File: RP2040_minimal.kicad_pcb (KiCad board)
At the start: 2 copper layers, 52 x 51 mm, 34 parts, among them J1 USB_B_Micro, J2 Conn_01x02, J3 Conn_02x18_Odd_Even, J4 Conn_02x18_Odd_Even, U1 NCP1117-3.3_SOT223, U2 W25Q128JVS, U3 RP2040, Y1 ABLS-12.000MHZ-B4-T

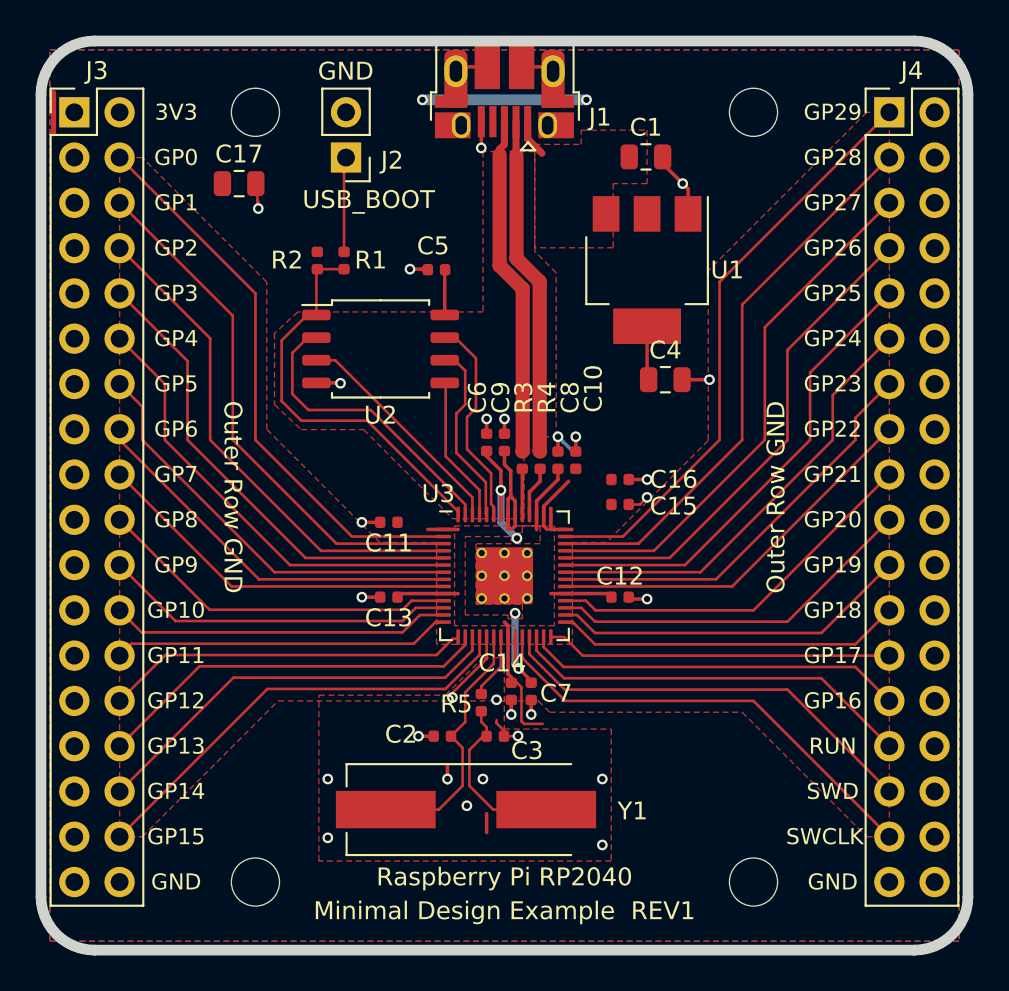
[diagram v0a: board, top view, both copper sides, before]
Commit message: get DRC passing
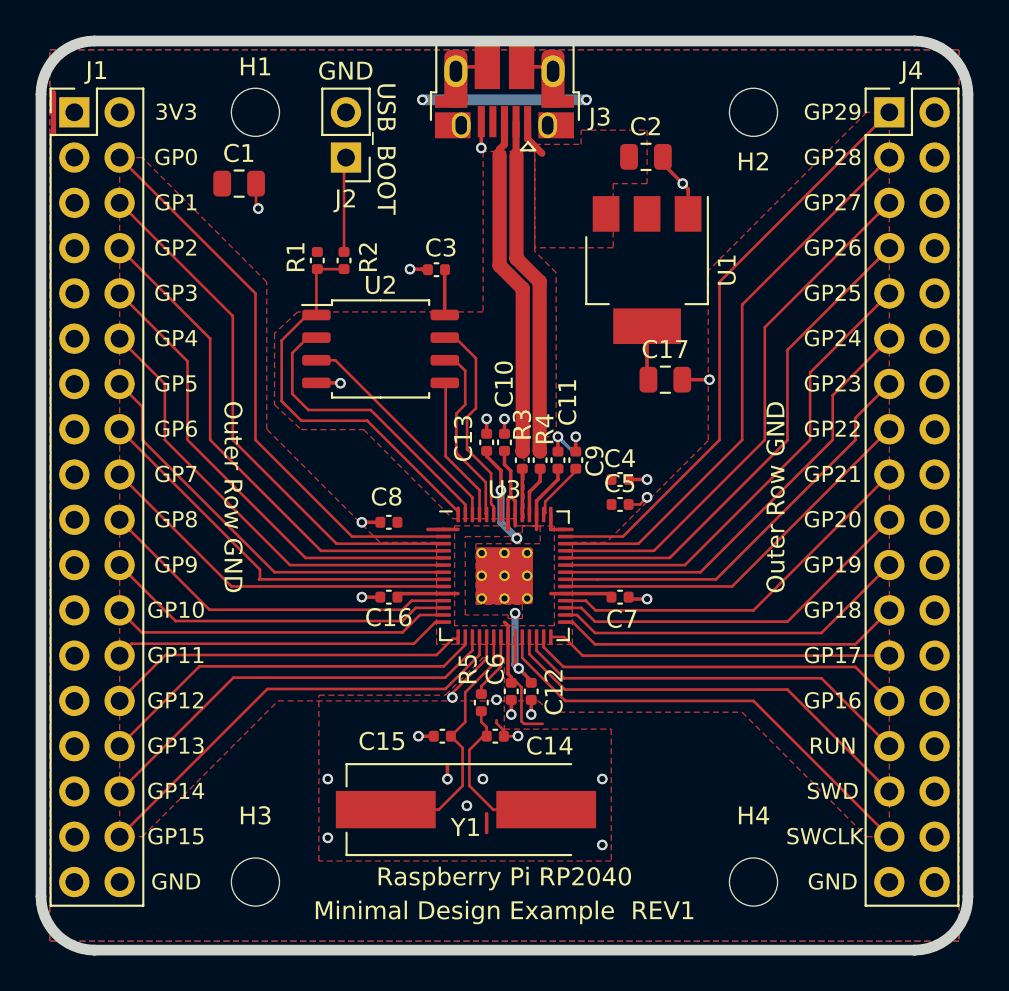
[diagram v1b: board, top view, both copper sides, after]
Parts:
- renumbered C17 to C1, C9 to C10, C8 to C11, C7 to C12, C6 to C13, C3 to C14, C2 to C15, C13 to C16, C4 to C17, C1 to C2, C5 to C3, C16 to C4, C15 to C5, C14 to C6, C12 to C7, C11 to C8, C10 to C9, H4 to H3, H3 to H4, J3 to J1, J1 to J3, R2 to R1, R1 to R2
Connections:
- net /~USB_BOOT renamed /~{USB_BOOT}
- J3 pad 4: Net-(J1-Pad4) -> unconnected-(J3-ID-Pad4)
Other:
- net class Default removed
- net class USB_DIFF_90 removed
